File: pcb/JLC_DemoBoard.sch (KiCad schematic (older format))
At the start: 3 parts

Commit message: Changed battery footprint
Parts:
- BT1: footprint Battery:BatteryHolder_Keystone_1058_1x2032 -> LCSC_Parts:BatteryHolder_2032
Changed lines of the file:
@@
 F 0 "BT1" H 5018 3946 50  0000 L CNN
 F 1 "Battery_Cell" H 5018 3855 50  0000 L CNN
-F 2 "Battery:BatteryHolder_Keystone_1058_1x2032" V 4900 3910 50  0001 C CNN
+F 2 "LCSC_Parts:BatteryHolder_2032" V 4900 3910 50  0001 C CNN
 F 3 "~" V 4900 3910 50  0001 C CNN
 F 4 "C70377" H 4900 3850 50  0001 C CNN "lcsc"

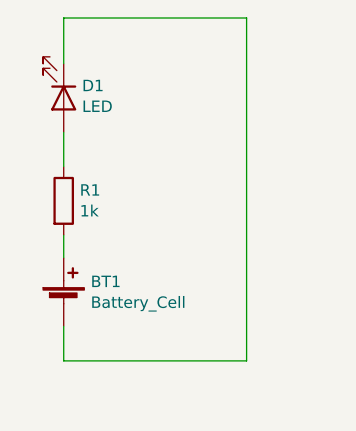
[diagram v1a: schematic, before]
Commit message: Added GND planes
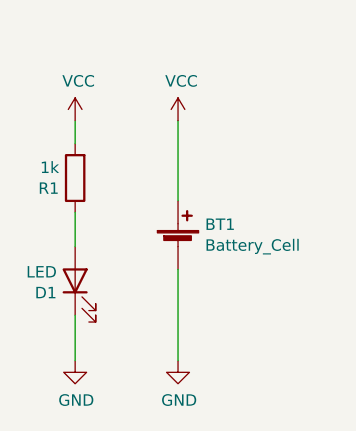
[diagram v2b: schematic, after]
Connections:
- net VCC: now reaches BT1.1 (+), R1.2
- net GND: now reaches BT1.2 (-), D1.1 (K)
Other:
- moved on the sheet: BT1, D1, R1
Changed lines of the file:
@@
 L Device:Battery_Cell BT1
 U 1 1 606D985D
-P 4900 3850
-F 0 "BT1" H 5018 3946 50  0000 L CNN
-F 1 "Battery_Cell" H 5018 3855 50  0000 L CNN
-F 2 "LCSC_Parts:BatteryHolder_2032" V 4900 3910 50  0001 C CNN
-F 3 "~" V 4900 3910 50  0001 C CNN
-F 4 "C70377" H 4900 3850 50  0001 C CNN "lcsc"
-	1    4900 3850
+P 5400 3600
+F 0 "BT1" H 5518 3696 50  0000 L CNN
+F 1 "Battery_Cell" H 5518 3605 50  0000 L CNN
+F 2 "LCSC_Parts:BatteryHolder_2032" V 5400 3660 50  0001 C CNN
+F 3 "~" V 5400 3660 50  0001 C CNN
+F 4 "C70377" H 5400 3600 50  0001 C CNN "lcsc"
+	1    5400 3600
 	1    0    0    -1
 $EndComp
@@
 L Device:R R1
 U 1 1 606DA6A2
-P 4900 3400
-F 0 "R1" H 4970 3446 50  0000 L CNN
-F 1 "1k" H 4970 3355 50  0000 L CNN
-F 2 "Resistor_SMD:R_0805_2012Metric_Pad1.20x1.40mm_HandSolder" V 4830 3400 50  0001 C CNN
-F 3 "~" H 4900 3400 50  0001 C CNN
-F 4 "C17513" H 4900 3400 50  0001 C CNN "lcsc"
-	1    4900 3400
-	1    0    0    -1
+P 4950 3300
+F 0 "R1" H 5020 3346 50  0000 L CNN
+F 1 "1k" H 5020 3255 50  0000 L CNN
+F 2 "Resistor_SMD:R_0805_2012Metric_Pad1.20x1.40mm_HandSolder" V 4880 3300 50  0001 C CNN
+F 3 "~" H 4950 3300 50  0001 C CNN
+F 4 "C17513" H 4950 3300 50  0001 C CNN "lcsc"
+	1    4950 3300
+	-1   0    0    1
 $EndComp
 $Comp
 L Device:LED D1
 U 1 1 606DB643
-P 4900 2950
-F 0 "D1" V 4847 3030 50  0000 L CNN
-F 1 "LED" V 4938 3030 50  0000 L CNN
-F 2 "LED_SMD:LED_0805_2012Metric_Pad1.15x1.40mm_HandSolder" H 4900 2950 50  0001 C CNN
-F 3 "~" H 4900 2950 50  0001 C CNN
-F 4 "C84256" V 4900 2950 50  0001 C CNN "lcsc"
-	1    4900 2950
-	0    1    1    0
+P 4950 3750
+F 0 "D1" V 4897 3830 50  0000 L CNN
+F 1 "LED" V 4988 3830 50  0000 L CNN
+F 2 "LED_SMD:LED_0805_2012Metric_Pad1.15x1.40mm_HandSolder" H 4950 3750 50  0001 C CNN
+F 3 "~" H 4950 3750 50  0001 C CNN
+F 4 "C84256" V 4950 3750 50  0001 C CNN "lcsc"
+	1    4950 3750
+	0    -1   -1   0
 $EndComp
 Wire Wire Line
-	4900 3100 4900 3250
+	4950 3600 4950 3450
 Wire Wire Line
-	4900 3550 4900 3650
+	4950 3150 4950 3050
 Wire Wire Line
-	4900 3950 4900 4100
+	4950 4100 4950 3900
+$Comp
+L power:VCC #PWR?
+U 1 1 606DA90D
+P 5400 3050
+F 0 "#PWR?" H 5400 2900 50  0001 C CNN
+F 1 "VCC" H 5415 3223 50  0000 C CNN
+F 2 "" H 5400 3050 50  0001 C CNN
+F 3 "" H 5400 3050 50  0001 C CNN
+	1    5400 3050
+	1    0    0    -1
+$EndComp
 Wire Wire Line
-	4900 4100 5700 4100
+	5400 3050 5400 3400
 Wire Wire Line
-	5700 4100 5700 2600
-Wire Wire Line
-	5700 2600 4900 2600
-Wire Wire Line
-	4900 2600 4900 2800
+	5400 3700 5400 4100
+$Comp
+L power:GND #PWR?
+U 1 1 606DB1D4
+P 5400 4100
+F 0 "#PWR?" H 5400 3850 50  0001 C CNN
+F 1 "GND" H 5405 3927 50  0000 C CNN
+F 2 "" H 5400 4100 50  0001 C CNN
+F 3 "" H 5400 4100 50  0001 C CNN
+	1    5400 4100
+	1    0    0    -1
+$EndComp
+$Comp
+L power:VCC #PWR?
+U 1 1 606DB8C5
+P 4950 3050
+F 0 "#PWR?" H 4950 2900 50  0001 C CNN
+F 1 "VCC" H 4965 3223 50  0000 C CNN
+F 2 "" H 4950 3050 50  0001 C CNN
+F 3 "" H 4950 3050 50  0001 C CNN
+	1    4950 3050
+	1    0    0    -1
+$EndComp
+$Comp
+L power:GND #PWR?
+U 1 1 606DCC8F
+P 4950 4100
+F 0 "#PWR?" H 4950 3850 50  0001 C CNN
+F 1 "GND" H 4955 3927 50  0000 C CNN
+F 2 "" H 4950 4100 50  0001 C CNN
+F 3 "" H 4950 4100 50  0001 C CNN
+	1    4950 4100
+	1    0    0    -1
+$EndComp
 $EndSCHEMATC
